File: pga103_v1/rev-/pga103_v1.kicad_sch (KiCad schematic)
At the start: 29 parts, among them J1 RF_IN, J2 RF_OUT, U1 SPX3819M5-L-5-0, U2 PGA-103

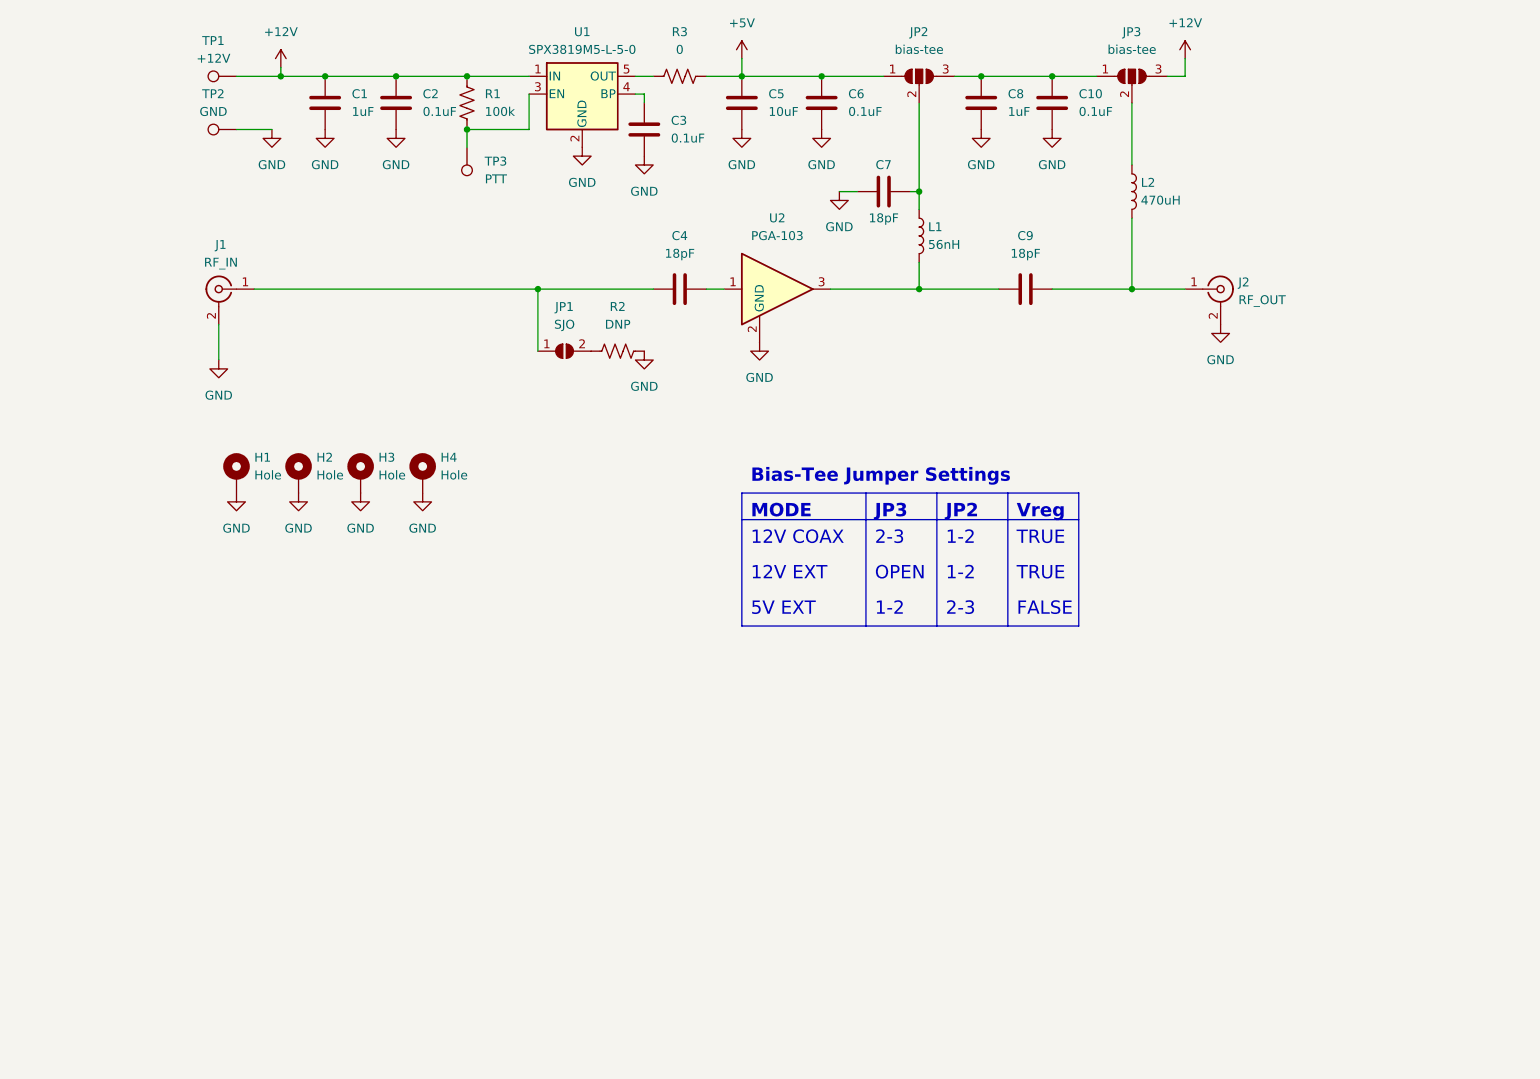
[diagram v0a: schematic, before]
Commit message: updating board edge and adding shielding
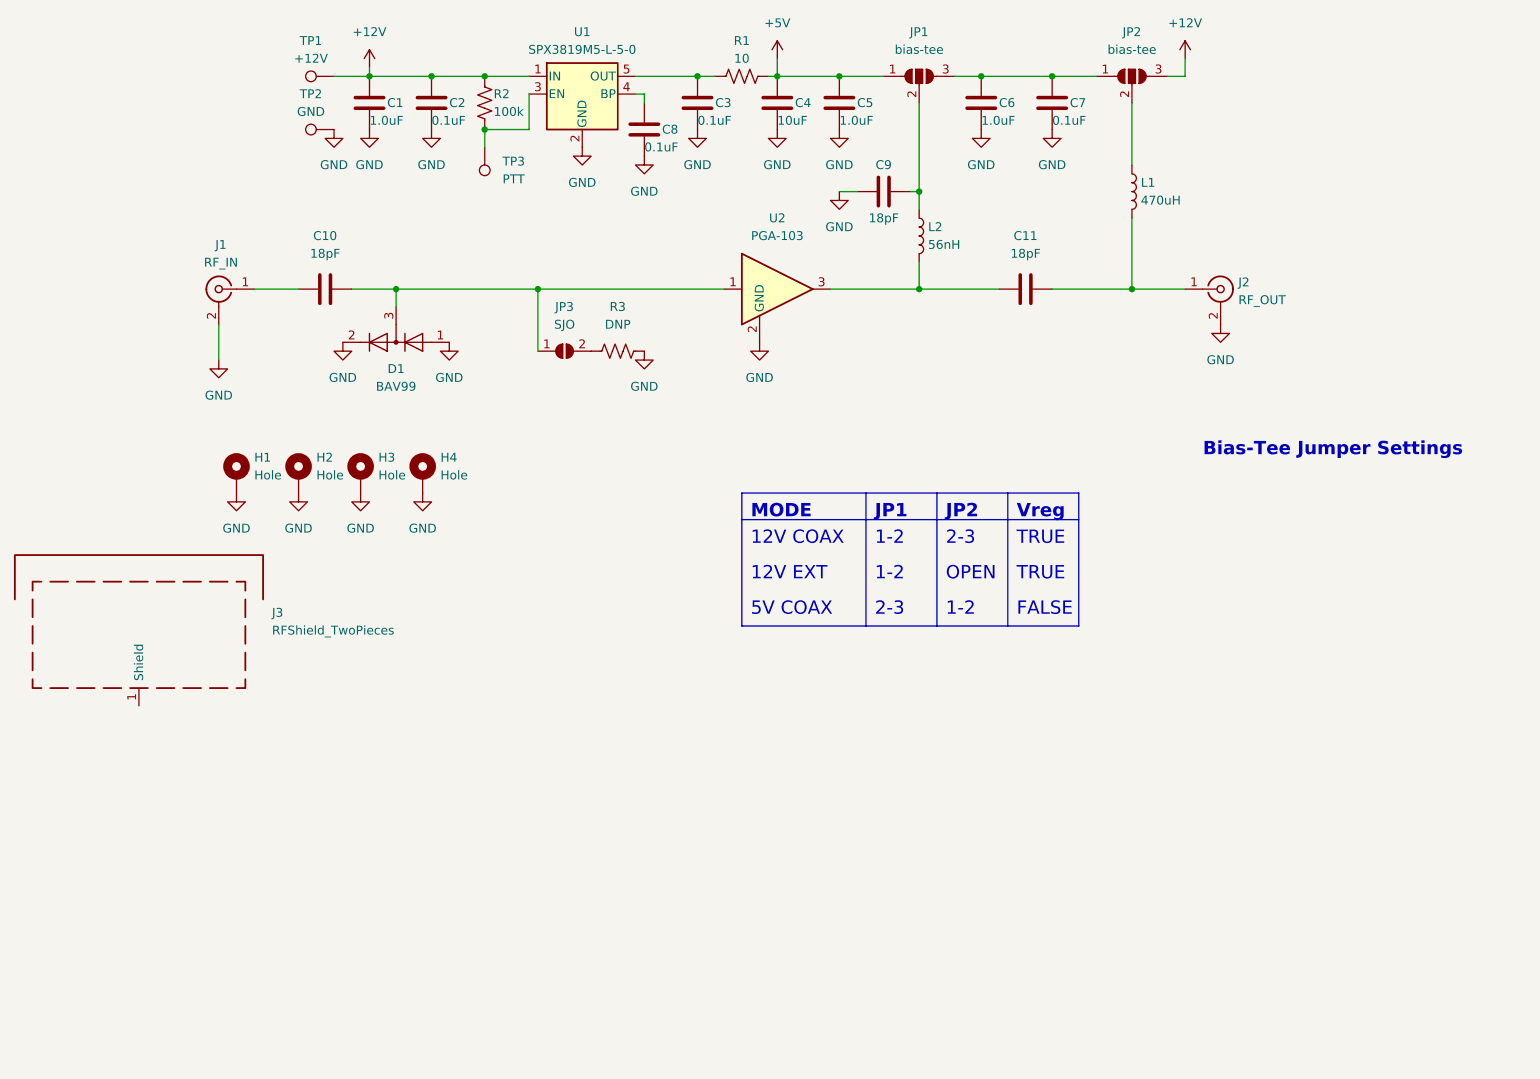
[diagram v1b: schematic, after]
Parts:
- added C3: 0.1uF, digikey-footprints:0805, symbol Device:C
- added D1: BAV99, Package_TO_SOT_SMD:SOT-23, symbol Diode:BAV99
- added J3: RFShield_TwoPieces, RF_Shielding:Wuerth_36103205_20x20mm, symbol Device:RFShield_TwoPieces
- C1: value 1uF -> 1.0uF
- C5: renamed from C6; value 0.1uF -> 1.0uF
- C6: renamed from C8; value 1uF -> 1.0uF
- H1, H2, H3, H4: footprint MountingHole:MountingHole_2.5mm_Pad_Via -> TestPoint:TestPoint_Plated_Hole_D3.0mm
- R1: renamed from R3; value 0 -> 10
- renumbered C4 to C10, C9 to C11, C5 to C4, C10 to C7, C3 to C8, C7 to C9, JP2 to JP1, JP3 to JP2, JP1 to JP3, L2 to L1, L1 to L2, R1 to R2, R2 to R3
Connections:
- net GND: now also C3.1, D1.1 (K), D1.2 (A)
- net at C10.1, J1.1 (In): no longer JP3.1 (A)
- net at R1.1, U1.5 (OUT): now also C3.2
- net at C10.2, U2.1: now also JP3.1 (A), D1.3 (K)
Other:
- note added: "5V COAX"
- note added: "JP1"
- note removed: "5V EXT"
- note removed: "JP3"
- moved on the sheet: C1, C10, C2, C4, C5, R1, R2, TP1, TP2, TP3

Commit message: finalized V1 schematic and board
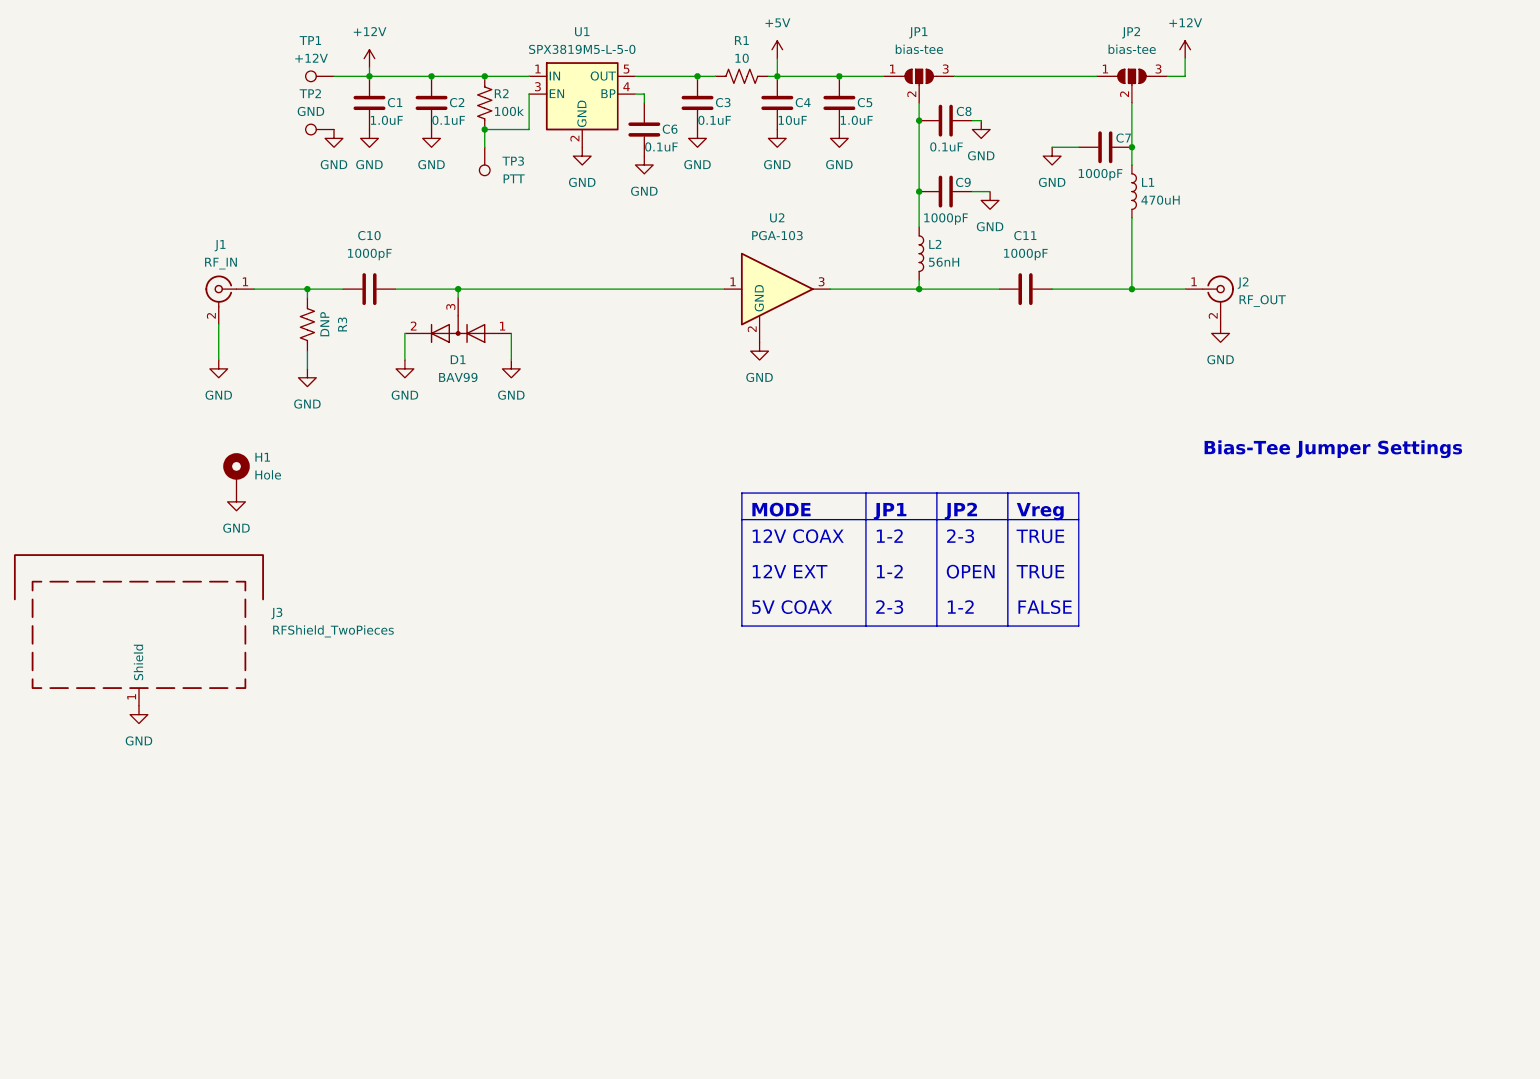
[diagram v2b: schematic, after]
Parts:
- removed H2, H3, H4: Hole, TestPoint:TestPoint_Plated_Hole_D3.0mm, symbol Mechanical:MountingHole_Pad
- removed JP3: SJO, Jumper:SolderJumper-2_P1.3mm_Open_RoundedPad1.0x1.5mm, symbol Jumper:SolderJumper_2_Open
- C10, C11, C9: value 18pF -> 1000pF
- C7: renamed from C6; value 1.0uF -> 1000pF
- H1: footprint TestPoint:TestPoint_Plated_Hole_D3.0mm -> TestPoint:TestPoint_Plated_Hole_D4.0mm
- renumbered C8 to C6, C7 to C8
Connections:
- net GND: now also C7.2, J3.1 (Shield); no longer C7.1
- net at C9.2, JP1.2 (C), L2.1: now also C8.2
- net at C10.1, J1.1 (In): now also R3.1
- net at JP2.2 (C), L1.1: now also C7.1
- net at JP1.3 (B), JP2.1 (A): no longer C7.2, C8.2
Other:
- moved on the sheet: C10, C7, C8, C9, D1, L2, R3

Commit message: forgot to save last commit.....
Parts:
- L1: value 470uH -> 220nH
- L2: value 56nH -> 220nH
- renumbered C8 to C6, C6 to C7, C9 to C8, C7 to C9
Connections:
- net at C10.1, J1.1 (In), R3.1: now also D1.3 (K)
- net at C10.2, U2.1: no longer D1.3 (K)
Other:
- note added: "1000pF"
- note added: "220nH"
- note added: "330nH"
- note added: "330pF"
- note added: "Band"
- note added: "C8-C11"
- note added: "C8-C11, L1-L2 Values"
- note added: "D1 is a double backed diode for ESD protection and very limited lightning protection (surge protection). Use of this should be balanced against potential for noise figure increase (to be tested). Different diodes other than BAV99 with same footprint may also be tested."
- note added: "L1, L2"
- note added: "R3 & D1 are optional for ESD and static protection"
- note added: "R3 is for static bleed, expected value 1 MOhm. Use with antenna systems that do not provide DC path to ground at Feedpoint (e.g. Gamma or T-Matches)."
- note added: "R3,D1 NOTE:"
- note added: "UHF"
- note added: "VHF"
- moved on the sheet: C10, C9, H1, J3, L1
